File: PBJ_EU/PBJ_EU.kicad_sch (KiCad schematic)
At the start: 82 parts, among them J1 Molex_47257, J10 Conn_02x05_Odd_Even, J2 Molex_47257, J3 Molex_47257, J4 Molex_47257, J7 Conn_02x05_Odd_Even, J9 Conn_02x08_Odd_Even_Female, SW1 SW_SPDT, SW2 SW_SPDT, SW5 SW_DPST, U1 TL072, U2 TL072, U7 MC7805CTG

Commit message: Adds BOM
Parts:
- GR1, GR2, H1, H2, H3, H4: now left out of the parts list
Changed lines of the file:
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@@
   )
   (symbol (lib_id "greenface-symbols:small_logo") (at 38.1 116.205 0) (unit 1)
-    (in_bom yes) (on_board yes)
+    (in_bom no) (on_board yes)
     (property "Reference" "GR1" (id 0) (at 38.1 110.744 0))
     (property "Value" "small_logo" (id 1) (at 38.1 113.0554 0))
@@
   )
   (symbol (lib_id "Mechanical:MountingHole_Pad") (at 217.17 144.78 0) (unit 1)
-    (in_bom yes) (on_board yes)
+    (in_bom no) (on_board yes)
     (property "Reference" "H1" (id 0) (at 219.71 144.7038 0)
       (effects (font (size 1.27 1.27)) (justify left))
@@
   )
   (symbol (lib_id "Mechanical:MountingHole_Pad") (at 224.79 144.78 0) (unit 1)
-    (in_bom yes) (on_board yes)
+    (in_bom no) (on_board yes)
     (property "Reference" "H2" (id 0) (at 227.33 144.7038 0)
       (effects (font (size 1.27 1.27)) (justify left))
@@
   )
   (symbol (lib_id "Mechanical:MountingHole_Pad") (at 232.41 144.78 0) (unit 1)
-    (in_bom yes) (on_board yes)
+    (in_bom no) (on_board yes)
     (property "Reference" "H3" (id 0) (at 234.95 144.7038 0)
       (effects (font (size 1.27 1.27)) (justify left))
@@
   )
   (symbol (lib_id "Mechanical:MountingHole_Pad") (at 240.03 144.78 0) (unit 1)
-    (in_bom yes) (on_board yes)
+    (in_bom no) (on_board yes)
     (property "Reference" "H4" (id 0) (at 242.57 144.7038 0)
       (effects (font (size 1.27 1.27)) (justify left))
@@
   )
   (symbol (lib_id "greenface-symbols:small_logo") (at 38.1 128.905 0) (unit 1)
-    (in_bom yes) (on_board yes)
+    (in_bom no) (on_board yes)
     (property "Reference" "GR2" (id 0) (at 38.1 123.444 0))
     (property "Value" "big_logo" (id 1) (at 38.1 125.7554 0))

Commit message: Version 4.10
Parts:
- U7: footprint Package_TO_SOT_THT:TO-220-3_Vertical -> Package_TO_SOT_THT:TO-220-3_Horizontal_TabDown
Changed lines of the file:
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@@
     (property "Reference" "U7" (id 0) (at 96.52 166.5732 0))
     (property "Value" "MC7805CTG" (id 1) (at 96.52 168.8846 0))
-    (property "Footprint" "Package_TO_SOT_THT:TO-220-3_Vertical" (id 2) (at 96.52 172.72 0)
+    (property "Footprint" "Package_TO_SOT_THT:TO-220-3_Horizontal_TabDown" (id 2) (at 96.52 172.72 0)
       (effects (font (size 1.27 1.27)) hide)
     )
@@
     )
     (path "/00000000-0000-0000-0000-00005fcfea15"
-      (reference "U7") (unit 1) (value "MC7805CTG") (footprint "Package_TO_SOT_THT:TO-220-3_Vertical")
-    )
-  )
+      (reference "U7") (unit 1) (value "MC7805CTG") (footprint "Package_TO_SOT_THT:TO-220-3_Horizontal_TabDown")
+    )
+  )

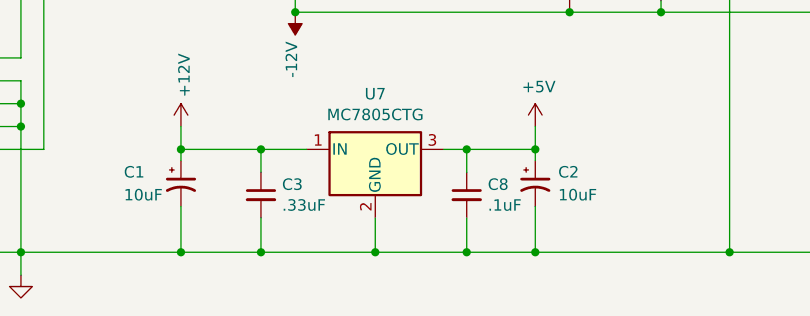
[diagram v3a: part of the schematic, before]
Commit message: Adds note to schematic about 3.3V regulator option
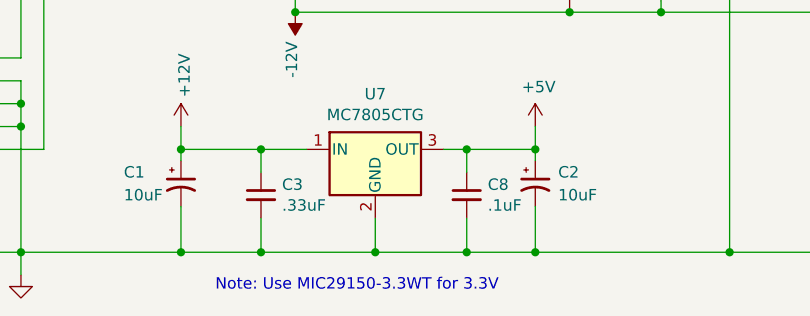
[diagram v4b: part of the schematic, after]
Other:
- note added: "Note: Use MIC29150-3.3WT for 3.3V"
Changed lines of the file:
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@@
+    (effects (font (size 1.27 1.27)) (justify left bottom))
+  )
+  (text "Note: Use MIC29150-3.3WT for 3.3V" (at 78.74 188.595 0)
     (effects (font (size 1.27 1.27)) (justify left bottom))
   )

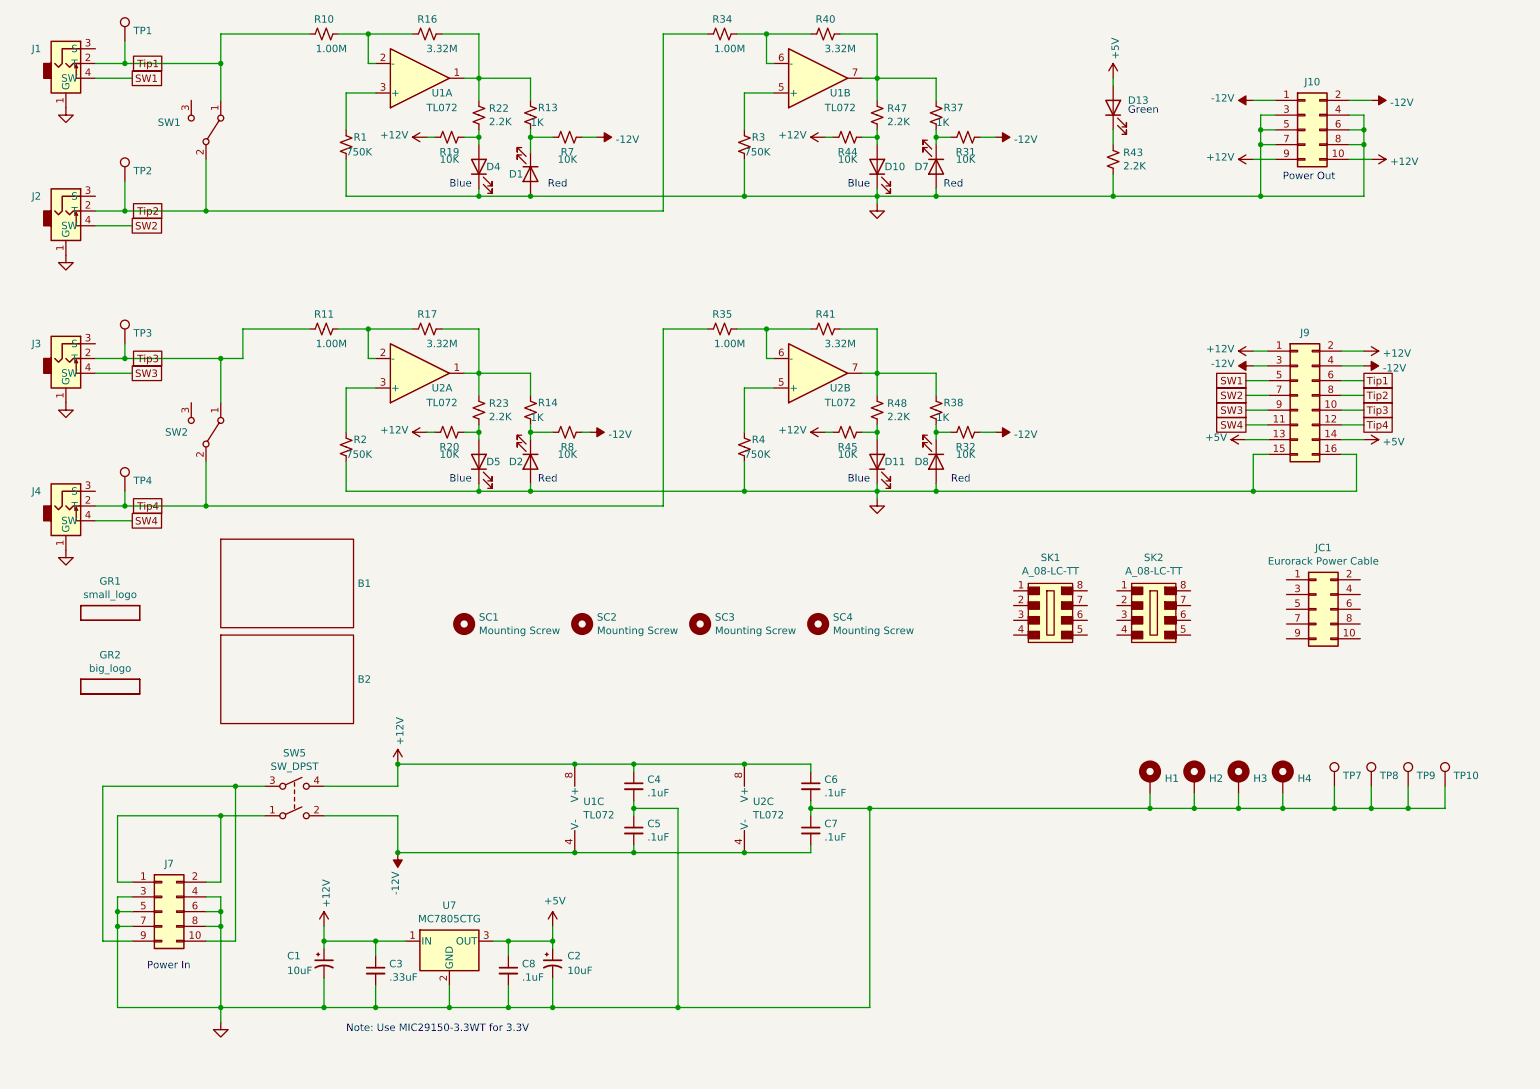
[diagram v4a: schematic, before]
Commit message: v5.2
Adds LCSC build support. Fixes to monitor circuitry.
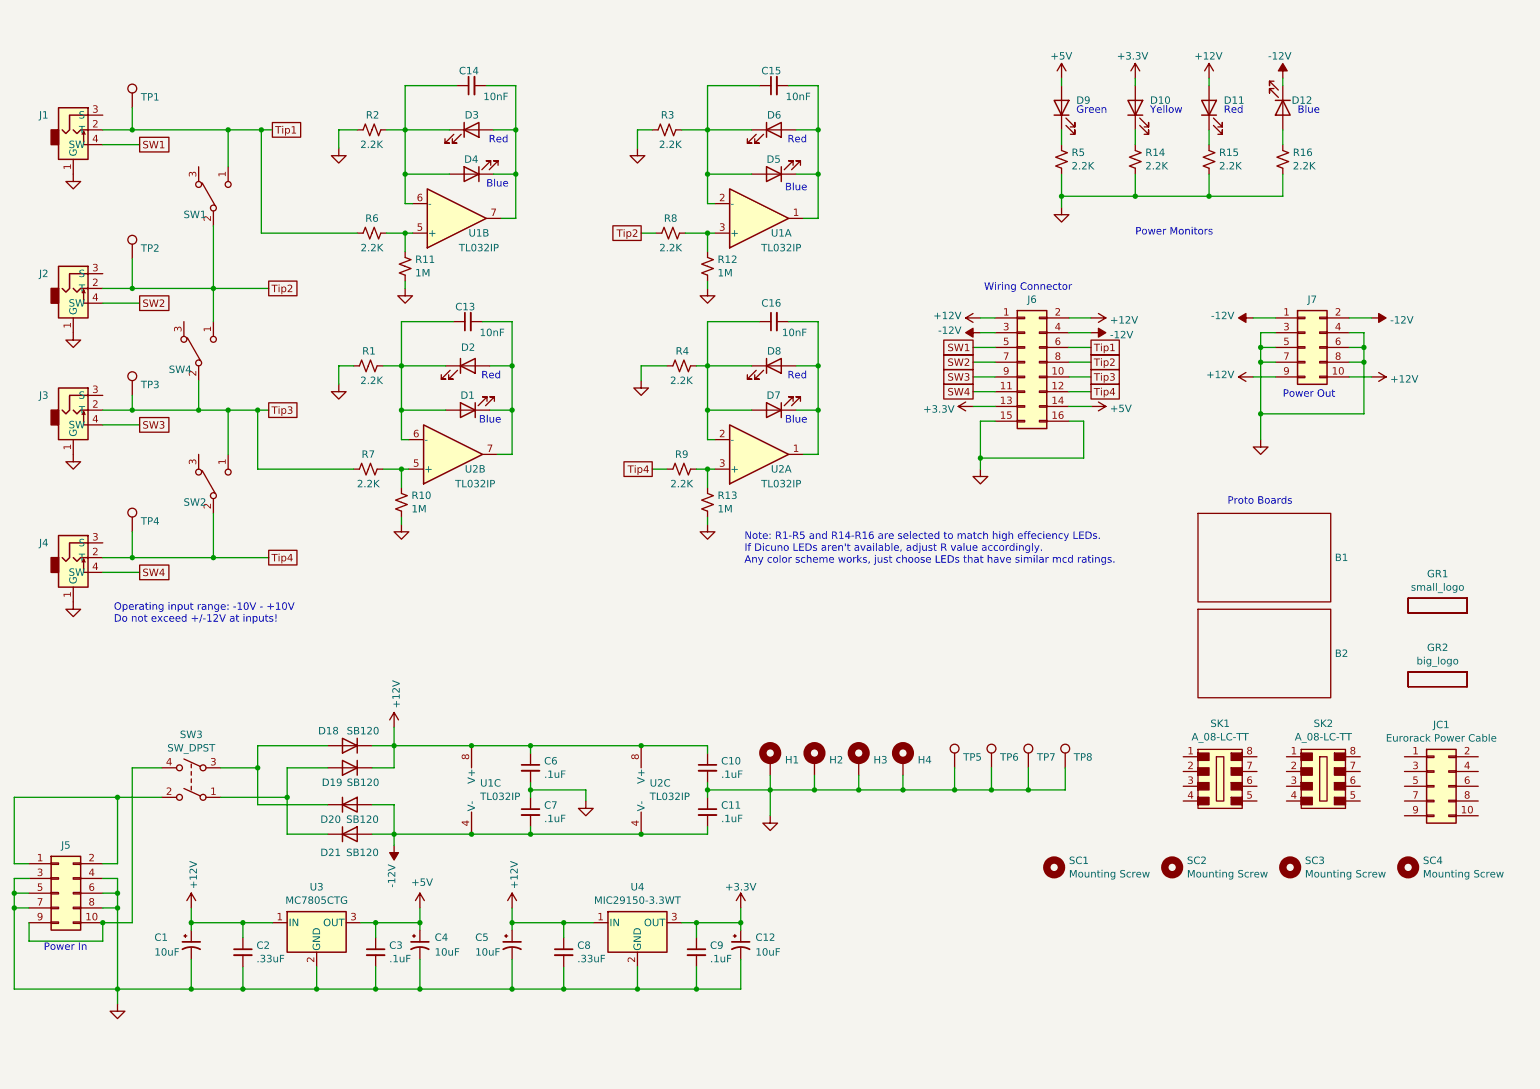
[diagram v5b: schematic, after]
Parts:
- removed R17, R40, R41: 3.32M, Resistor_THT:R_Axial_DIN0207_L6.3mm_D2.5mm_P10.16mm_Horizontal, symbol Device:R_Small_US
- removed R19, R20, R31, R32, R44, R45: 10K, Resistor_THT:R_Axial_DIN0207_L6.3mm_D2.5mm_P10.16mm_Horizontal, symbol Device:R_Small_US
- removed R2: 750K, Resistor_THT:R_Axial_DIN0207_L6.3mm_D2.5mm_P10.16mm_Horizontal, symbol Device:R_Small_US
- removed R22, R23, R47, R48: 2.2K, Resistor_THT:R_Axial_DIN0207_L6.3mm_D2.5mm_P10.16mm_Horizontal, symbol Device:R_Small_US
- removed R34, R35: 1.00M, Resistor_THT:R_Axial_DIN0207_L6.3mm_D2.5mm_P10.16mm_Horizontal, symbol Device:R_Small_US
- removed R37, R38: 1K, Resistor_THT:R_Axial_DIN0207_L6.3mm_D2.5mm_P10.16mm_Horizontal, symbol Device:R_Small_US
- removed unit 2 of U1
- added C12, C5: 10uF, Capacitor_THT:CP_Radial_Tantal_D5.0mm_P5.00mm, symbol Device:CP1_Small
- added C13, C14, C15, C16: 10nF, Capacitor_THT:C_Rect_L7.0mm_W2.0mm_P5.00mm, symbol Device:C_Small
- added C8: .33uF, Capacitor_THT:C_Rect_L7.0mm_W2.0mm_P5.00mm, symbol Device:C_Small
- added C9: .1uF, Capacitor_THT:C_Rect_L7.0mm_W2.0mm_P5.00mm, symbol Device:C_Small
- added D1, D12: BLUE LED, LED_THT:LED_D3.0mm, symbol Device:LED
- added D18, D19, D20, D21: SB120, Diode_THT:D_DO-41_SOD81_P7.62mm_Horizontal, symbol Diode:1N4148
- added D6: RED LED, LED_THT:LED_D3.0mm, symbol Device:LED
- added R12, R13: 1M, Resistor_THT:R_Axial_DIN0207_L6.3mm_D2.5mm_P10.16mm_Horizontal, symbol Device:R_Small_US
- added R15, R6, R9: 2.2K, Resistor_THT:R_Axial_DIN0207_L6.3mm_D2.5mm_P10.16mm_Horizontal, symbol Device:R_Small_US
- added SW4: SW_SPDT, Button_Switch_THT:SW_Slide_1P2T_CK_OS102011MS2Q, symbol Switch:SW_SPDT
- added unit 1 of U1
- added U4: MIC29150-3.3WT, Package_TO_SOT_THT:TO-220-3_Vertical, symbol Regulator_Linear:L7805
- C1: LCSC Part # (none) -> C45669
- C10: renamed from C6; LCSC Part # (none) -> C84772
- C11: renamed from C7; LCSC Part # (none) -> C84772
- C2: renamed from C3; LCSC Part # (none) -> C128043
- C3: renamed from C8; LCSC Part # (none) -> C84772
- C4: renamed from C2; LCSC Part # (none) -> C45669
- C6: renamed from C4; LCSC Part # (none) -> C84772
- C7: renamed from C5; LCSC Part # (none) -> C84772
- D10: value BLUE LED -> YELLOW LED; Digi-Key Part 732-11401-ND -> (none); Other (none) -> https://www.amazon.com/dp/B077J2WJRS/
- D11: value BLUE LED -> RED LED; Digi-Key Part 732-11401-ND -> (none); Other (none) -> https://www.amazon.com/dp/B077J2WJRS/
- D2, D8: Digi-Key Part 732-5005-ND -> (none); Other (none) -> https://www.amazon.com/dp/B077J2WJRS/
- D3: renamed from D1; Digi-Key Part 732-5005-ND -> (none); Other (none) -> https://www.amazon.com/dp/B077J2WJRS/
- D4, D5: Digi-Key Part 732-11401-ND -> (none); Other (none) -> https://www.amazon.com/dp/B077J2WJRS/
- D7: value RED LED -> BLUE LED; Digi-Key Part 732-5005-ND -> (none); Other (none) -> https://www.amazon.com/dp/B077J2WJRS/
- D9: renamed from D13; Digi-Key Part 732-5008-ND -> (none); Other (none) -> https://www.amazon.com/dp/B077J2WJRS/
- J5: renamed from J7; LCSC Part # (none) -> C492422
- R1, R3, R4: value 750K -> 2.2K; Digi-Key Part S750KQCT-ND -> CF14JT2K20CT-ND; LCSC Part # (none) -> C120063
- R10, R11: value 1.00M -> 1M; Digi-Key Part RNF14FTD1M00CT-ND -> CF14JT1M00CT-ND; LCSC Part # (none) -> C433776
- R14: value 1K -> 2.2K; Digi-Key Part CF14JT1K00CT-ND -> CF14JT2K20CT-ND; LCSC Part # (none) -> C120063
- R16: value 3.32M -> 2.2K; Digi-Key Part RNF14FTD3M32CT-ND -> CF14JT2K20CT-ND; LCSC Part # (none) -> C120063
- R2: renamed from R13; value 1K -> 2.2K; Digi-Key Part CF14JT1K00CT-ND -> CF14JT2K20CT-ND; LCSC Part # (none) -> C120063
- R5: renamed from R43; LCSC Part # (none) -> C120063
- R7, R8: value 10K -> 2.2K; Digi-Key Part CF14JT10K0CT-ND -> CF14JT2K20CT-ND; LCSC Part # (none) -> C120063
- SK1, SK2: LCSC Part # (none) -> C72124
- TP1, TP2, TP3, TP4: LCSC Part # (none) -> C238123
- TP5: renamed from TP7; Digi-Key Part 36-5006-ND -> (none)
- TP6: renamed from TP8; Digi-Key Part 36-5006-ND -> (none)
- TP7: renamed from TP9; Digi-Key Part 36-5006-ND -> (none)
- TP8: renamed from TP10; Digi-Key Part 36-5006-ND -> (none)
- U1, U2: value TL072 -> TL032IP; footprint (none) -> Package_DIP:DIP-8_W7.62mm_Socket_LongPads; Digi-Key Part (none) -> 296-7151-5-ND
- U1: value TL072 -> TL032IP; footprint Package_DIP:DIP-8_W7.62mm -> Package_DIP:DIP-8_W7.62mm_Socket_LongPads; Digi-Key Part 296-14997-5-ND -> 296-7151-5-ND
- U2: value TL072 -> TL032IP; footprint Package_DIP:DIP-8_W7.62mm -> Package_DIP:DIP-8_W7.62mm_Socket_LongPads; Digi-Key Part 296-14997-5-ND‎ -> 296-7151-5-ND
- U3: renamed from U7; footprint Package_TO_SOT_THT:TO-220-3_Horizontal_TabDown -> Package_TO_SOT_THT:TO-220-3_Vertical; LCSC Part # (none) -> C71462
- renumbered J9 to J6, J10 to J7, SW5 to SW3
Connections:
- net +12V: now also D11.2 (A), C5.1, C8.1, D18.1 (K), D19.1 (K), U4.1 (IN); no longer SW3.4
- net +5V: no longer J6.13 (Pin_13)
- net -12V: now also D12.1 (K), D20.2 (A), D21.2 (A); no longer R7.2, R8.2, SW3.2
- net GND: now also R1.1, R10.2, R11.2, R14.2, R16.2, R2.1, R3.1, R4.1, C12.2, C5.2, C8.2, C9.2, R12.2, R13.2, R15.2, U4.2 (GND); no longer D10.1 (K), D11.1 (K), D2.2 (A), D3.2 (A), D4.1 (K), D5.1 (K), D7.2 (A), D8.2 (A), R1.2, R3.2, R4.2
- net Tip1: now also R6.2; no longer R10.1
- net Tip2: now also R8.2, SW4.1 (A)
- net Tip3: now also R7.2, SW4.2 (B); no longer R11.1
- net Tip4: now also R9.2
- net at U2.2 (-): now also D7.2 (A), D8.1 (K), R4.2, C16.1; no longer R11.2
- net at U2.6 (-): now also D2.1 (K), R1.2, C13.1, D1.2 (A)
- net at U2.7: now also D2.2 (A), C13.2, D1.1 (K)
- net at R14.1: now also D10.1 (K); no longer U2.1
- net at J5.1 (Pin_1), J5.2 (Pin_2): now also SW3.2; no longer SW3.1
- net at J5.10 (Pin_10), J5.9 (Pin_9): now also SW3.4; no longer SW3.3
- net at U2.3 (+): now also R13.1, R9.1
- net at D5.2 (A): now also R3.2, C15.1, D6.1 (K), U1.2 (-)
- net at U2.5 (+): now also R10.1, R7.1; no longer R4.1
- net at D4.2 (A): now also D3.1 (K), R2.2, U1.6 (-), C14.1
- net +3V3: now reaches D10.2 (A)
- net +3V3: now also J6.13 (Pin_13), C12.1, C9.1, U4.3 (OUT)
- net at D7.1 (K): now also D8.2 (A), U2.1, C16.2
- new net: D19.2 (A), D21.1 (K), SW3.1
- new net: D18.2 (A), D20.1 (K), SW3.3
- new net: R11.1, R6.1, U1.5 (+)
- new net: C14.2, D3.2 (A), D4.1 (K), U1.7
- new net: D11.1 (K), R15.1
- new net: R12.1, R8.1, U1.3 (+)
- new net: C15.2, D5.1 (K), D6.2 (A), U1.1
- new net: D12.2 (A), R16.1
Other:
- note added: "Note: R1-R5 and R14-R16 are selected to match high effeciency LEDs. If Dicuno LEDs aren't available, adjust R value accordingly. Any color scheme works, just choose LEDs that have similar mcd ratings."
- note added: "Operating input range: -10V - +10V Do not exceed +/-12V at inputs!"
- note added: "Power Monitors"
- note added: "Proto Boards"
- note added: "Wiring Connector"
- note added: "Yellow"
- note removed: "Note: Use MIC29150-3.3WT for 3.3V"
- company: (none) -> Greenface Labs
- moved on the sheet: B1, B2, C1, C10, C11, C2, C3, C4, C6, C7, D3, D4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

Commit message: Update PBJ_EU.kicad_sch
Testing branch
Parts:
- added U?: LM317_TO-220, Package_TO_SOT_THT:TO-220-3_Vertical, symbol Regulator_Linear:LM317_TO-220
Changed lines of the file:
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@@
     )
+  )
+  (symbol (lib_id "Regulator_Linear:LM317_TO-220") (at 73.66 188.595 0) (unit 1)
+    (in_bom yes) (on_board yes) (fields_autoplaced)
+    (property "Reference" "U?" (id 0) (at 73.66 182.7235 0))
+    (property "Value" "LM317_TO-220" (id 1) (at 73.66 185.4986 0))
+    (property "Footprint" "Package_TO_SOT_THT:TO-220-3_Vertical" (id 2) (at 73.66 182.245 0)
+      (effects (font (size 1.27 1.27) italic) hide)
+    )
+    (property "Datasheet" "http://www.ti.com/lit/ds/symlink/lm317.pdf" (id 3) (at 73.66 188.595 0)
+      (effects (font (size 1.27 1.27)) hide)
+    )
+    (pin "1")
+    (pin "2")
+    (pin "3")
   )
   (symbol (lib_id "Device:LED") (at 227.33 29.21 90) (unit 1)
@@
       (reference "U4") (unit 1) (value "MIC29150-3.3WT") (footprint "Package_TO_SOT_THT:TO-220-3_Vertical")
     )
-  )
+    (path "/2955508e-17c5-440d-b20a-6fbfd8a67494"
+      (reference "U?") (unit 1) (value "LM317_TO-220") (footprint "Package_TO_SOT_THT:TO-220-3_Vertical")
+    )
+  )

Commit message: lm317 experiment checkin
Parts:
- removed C3, C9: .1uF, Capacitor_THT:C_Rect_L7.0mm_W2.0mm_P5.00mm, symbol Device:C_Small
- removed U3: MC7805CTG, Package_TO_SOT_THT:TO-220-3_Vertical, symbol Regulator_Linear:L7805
- removed U4: MIC29150-3.3WT, Package_TO_SOT_THT:TO-220-3_Vertical, symbol Regulator_Linear:L7805
- added R17, R18: 620, Resistor_THT:R_Axial_DIN0207_L6.3mm_D2.5mm_P10.16mm_Horizontal, symbol Device:R_Small_US
- added RV1, RV2: 5K, Potentiometer_THT:Potentiometer_Bourns_3296W_Vertical, symbol Device:R_Potentiometer_Trim_US
- added U4: LM317_TO-220, Package_TO_SOT_THT:TO-220-3_Vertical, symbol Regulator_Linear:LM317_TO-220
- C1, C5: footprint Capacitor_THT:CP_Radial_Tantal_D5.0mm_P5.00mm -> Capacitor_THT:C_Radial_D5.0mm_H11.0mm_P2.00mm; Digi-Key Part 478-7366-1-ND -> P124234CT-ND; LCSC Part # C45669 -> C88726
- C12, C4: value 10uF -> 22uF; footprint Capacitor_THT:CP_Radial_Tantal_D5.0mm_P5.00mm -> Capacitor_THT:C_Radial_D5.0mm_H11.0mm_P2.00mm; Digi-Key Part 478-7366-1-ND -> P15374CT-ND; LCSC Part # C45669 -> C43346
- C2, C8: value .33uF -> .1uF; Digi-Key Part 445-180638-1-ND -> 478-3188-ND; LCSC Part # C128043 -> C84772
- SK1, SK2: footprint (none) -> Package_DIP:DIP-8_W7.62mm_Socket_LongPads
- U1, U2: value TL032IP -> TL072; Digi-Key Part 296-7151-5-ND -> 296-1775-5-ND; LCSC Part # (none) -> C72124
- U3: renamed from U?; Digi-Key Part (none) -> 497-19621-ND; LCSC Part # (none) -> C14502
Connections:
- net +12V: now also U3.3 (VI), U4.3 (VI); no longer C1.1, C5.1
- net +3V3: now also R18.1, U4.2 (VO)
- net +5V: now also U3.2 (VO), R17.1
- net GND: now also RV1.1, RV2.1
- net at U3.1 (ADJ): now also C1.1, R17.2, RV1.2, RV1.3
- new net: C5.1, R18.2, RV2.2, RV2.3, U4.1 (ADJ)
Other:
- note added: "EU Power In"
- note removed: "Power In"
- moved on the sheet: C1, C12, C2, C4, C5, C8, U3
